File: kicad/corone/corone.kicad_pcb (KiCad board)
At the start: 2 copper layers, 63.3 x 49.8 mm, 91 parts, among them J1 To main board, J2 SWD, J3 Debug UART, SW1 BOOT0, SW2 RESET, U1 AMS1117-5.0, U2 AP2112K-3.3, U3 ADS131A02IPBS, U4 DAC8565IAPW, U5 OPA4197, U6 OPA4197, U7 ADG1408YRUZ, U8 STM32F722RET6, U9 USBLC6-2SC6, Y1 8MHz

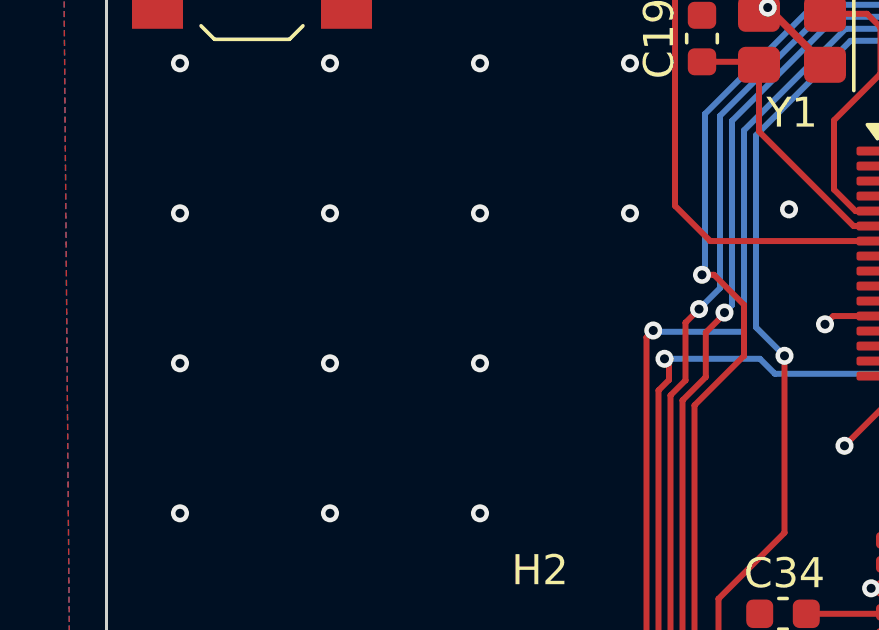
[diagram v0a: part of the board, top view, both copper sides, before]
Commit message: Moirae: name on the back by the mark; Corone back silk adjusted
Co-Authored-By: Claude Opus 5.5 <noreply@anthropic.com>
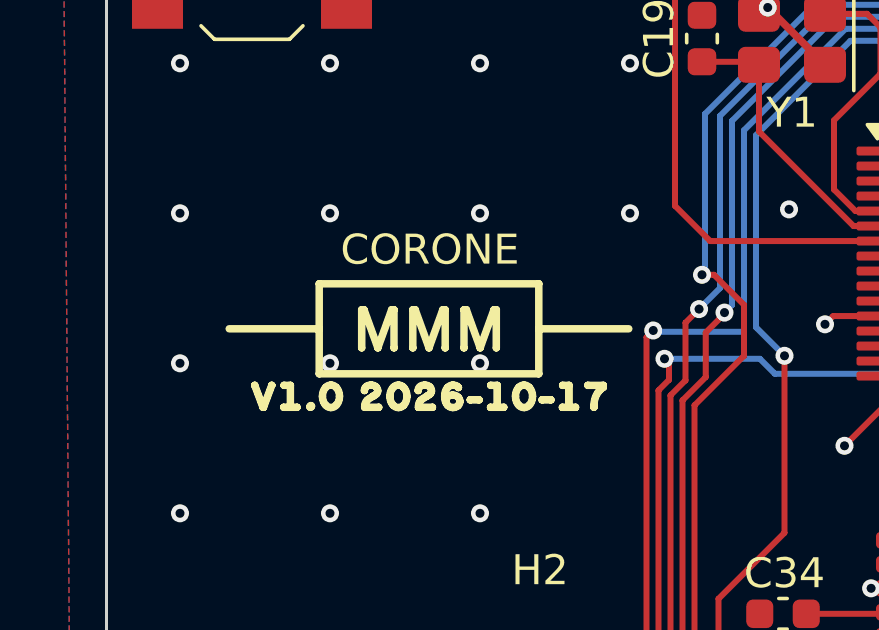
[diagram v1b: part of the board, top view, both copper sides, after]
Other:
- board text added: "CORONE"
